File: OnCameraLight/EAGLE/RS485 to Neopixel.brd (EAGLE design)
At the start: 42.6 x 35.5 mm, 10 parts, among them IC1 75176AP

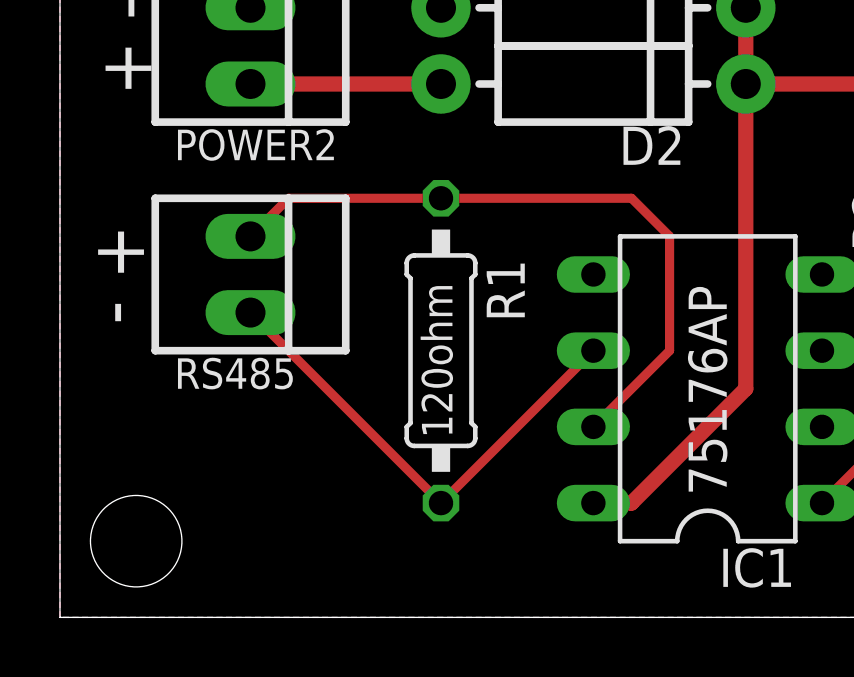
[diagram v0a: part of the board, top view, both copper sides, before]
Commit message: Go through and fix notation on RS485 wiring everywhere to use the standard A/B notation.
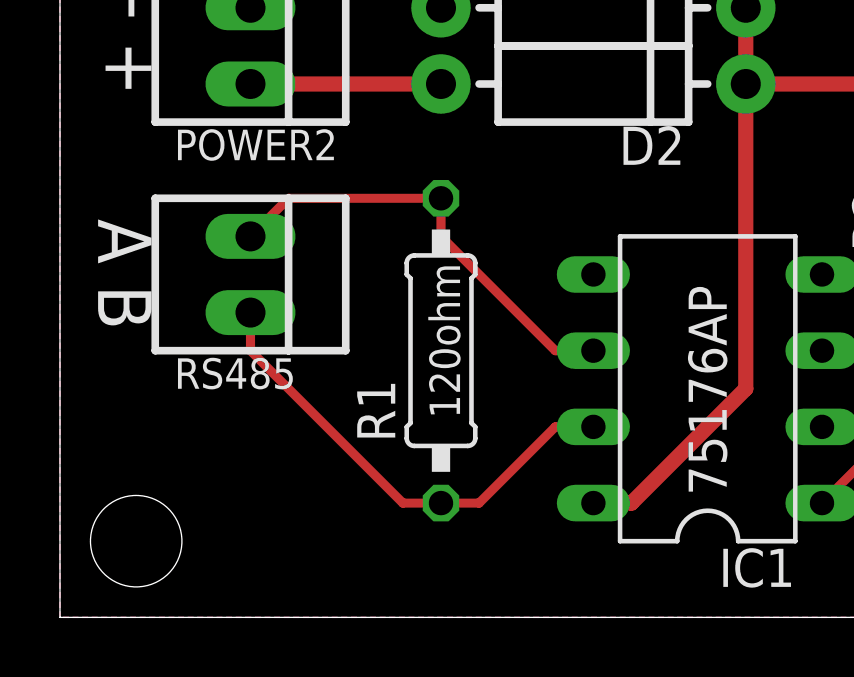
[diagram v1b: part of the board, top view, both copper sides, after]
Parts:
- turned R1 to 90 degrees
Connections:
- removed net RS485+: IC1.7, R1.1, RS485.1
- removed net RS485-: IC1.6, R1.2, RS485.2
- new net RS485A: IC1.6, R1.2, RS485.1
- new net RS485B: IC1.7, R1.1, RS485.2
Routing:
- net RS485+: track 22.4 -> 0.00 mm
- net RS485-: track 16.2 -> 0.00 mm
- net RS485B: track 0.00 -> 15.9 mm
- net RS485A: track 0.00 -> 14.8 mm
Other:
- board text added: "A B"
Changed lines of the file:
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@@
 <drawing>
 <settings>
-<setting alwaysvectorfont="yes"/>
+<setting alwaysvectorfont="no"/>
 <setting verticaltext="up"/>
 </settings>
@@
 <text x="1.27" y="24.13" size="1.778" layer="25" rot="R270" align="bottom-center">+ -</text>
 <text x="1.27" y="19.05" size="1.778" layer="25" rot="R270" align="bottom-center">+ -</text>
-<text x="1.27" y="11.43" size="1.778" layer="25" rot="SR270" align="bottom-center">+ -</text>
+<text x="1.27" y="11.43" size="1.778" layer="25" rot="SR270" align="bottom-center">A B</text>
 <text x="40.64" y="17.78" size="1.4224" layer="25" rot="R270" align="top-center">-  + D</text>
 <wire x1="15.24" y1="24.13" x2="36.83" y2="24.13" width="0.1524" layer="25"/>
@@
 <attribute name="VALUE" value="1A/50V/1.1V" x="12.28" y="14.78" size="1.27" layer="27" ratio="10" display="off"/>
 </element>
-<element name="R1" library="rcl" library_urn="urn:adsk.eagle:library:334" package="0207/10" package3d_urn="urn:adsk.eagle:package:23491/2" value="120ohm" x="12.7" y="8.89" smashed="yes" rot="R270">
-<attribute name="NAME" x="14.224" y="11.938" size="1.27" layer="25" ratio="10" rot="R270"/>
-<attribute name="POPULARITY" value="36" x="12.7" y="8.89" size="1.778" layer="27" rot="R270" display="off"/>
-<attribute name="SPICEPREFIX" value="R" x="12.7" y="8.89" size="1.778" layer="27" rot="R270" display="off"/>
-<attribute name="VALUE" x="12.065" y="11.1506" size="1.016" layer="25" ratio="10" rot="R270"/>
+<element name="R1" library="rcl" library_urn="urn:adsk.eagle:library:334" package="0207/10" package3d_urn="urn:adsk.eagle:package:23491/2" value="120ohm" x="12.7" y="8.89" smashed="yes" rot="R90">
+<attribute name="NAME" x="11.176" y="5.842" size="1.27" layer="25" ratio="10" rot="R90"/>
+<attribute name="POPULARITY" value="36" x="12.7" y="8.89" size="1.778" layer="27" rot="R90" display="off"/>
+<attribute name="SPICEPREFIX" value="R" x="12.7" y="8.89" size="1.778" layer="27" rot="R90" display="off"/>
+<attribute name="VALUE" x="13.335" y="6.6294" size="1.016" layer="25" ratio="10" rot="R90"/>
 </element>
 <element name="R2" library="rcl" library_urn="urn:adsk.eagle:library:334" package="0207/10" package3d_urn="urn:adsk.eagle:package:23491/2" value="470ohm" x="29.21" y="15.24" smashed="yes" rot="R90">
@@
 <wire x1="6.35" y1="17.78" x2="12.7" y2="17.78" width="0.508" layer="1"/>
 </signal>
-<signal name="RS485+">
-<contactref element="RS485" pad="1"/>
-<contactref element="R1" pad="1"/>
-<contactref element="IC1" pad="7"/>
-<wire x1="6.35" y1="12.7" x2="7.62" y2="13.97" width="0.3048" layer="1"/>
-<wire x1="7.62" y1="13.97" x2="12.7" y2="13.97" width="0.3048" layer="1"/>
-<wire x1="17.78" y1="6.35" x2="20.32" y2="8.89" width="0.3048" layer="1"/>
-<wire x1="20.32" y1="12.7" x2="19.05" y2="13.97" width="0.3048" layer="1"/>
-<wire x1="19.05" y1="13.97" x2="12.7" y2="13.97" width="0.3048" layer="1"/>
-<wire x1="20.32" y1="8.89" x2="20.32" y2="12.7" width="0.3048" layer="1"/>
-</signal>
-<signal name="RS485-">
-<contactref element="RS485" pad="2"/>
-<contactref element="R1" pad="2"/>
-<contactref element="IC1" pad="6"/>
-<wire x1="6.35" y1="10.16" x2="12.7" y2="3.81" width="0.3048" layer="1"/>
-<wire x1="12.7" y1="3.81" x2="17.78" y2="8.89" width="0.3048" layer="1"/>
-</signal>
 <signal name="NEOOUT">
 <contactref element="NEOPIXEL" pad="3"/>
@@
 <wire x1="29.21" y1="7.62" x2="25.4" y2="3.81" width="0.3048" layer="1"/>
 </signal>
+<signal name="RS485B">
+<contactref element="IC1" pad="7"/>
+<contactref element="R1" pad="1"/>
+<contactref element="RS485" pad="2"/>
+<wire x1="17.78" y1="6.35" x2="16.51" y2="6.35" width="0.3048" layer="1"/>
+<wire x1="16.51" y1="6.35" x2="13.97" y2="3.81" width="0.3048" layer="1"/>
+<wire x1="13.97" y1="3.81" x2="12.7" y2="3.81" width="0.3048" layer="1"/>
+<wire x1="12.7" y1="3.81" x2="11.43" y2="3.81" width="0.3048" layer="1"/>
+<wire x1="11.43" y1="3.81" x2="6.35" y2="8.89" width="0.3048" layer="1"/>
+<wire x1="6.35" y1="8.89" x2="6.35" y2="10.16" width="0.3048" layer="1"/>
+</signal>
+<signal name="RS485A">
+<contactref element="IC1" pad="6"/>
+<contactref element="R1" pad="2"/>
+<contactref element="RS485" pad="1"/>
+<wire x1="6.35" y1="12.7" x2="7.62" y2="13.97" width="0.3048" layer="1"/>
+<wire x1="7.62" y1="13.97" x2="12.7" y2="13.97" width="0.3048" layer="1"/>
+<wire x1="12.7" y1="13.97" x2="12.7" y2="12.7" width="0.3048" layer="1"/>
+<wire x1="12.7" y1="12.7" x2="16.51" y2="8.89" width="0.3048" layer="1"/>
+<wire x1="16.51" y1="8.89" x2="17.78" y2="8.89" width="0.3048" layer="1"/>
+</signal>
 </signals>
